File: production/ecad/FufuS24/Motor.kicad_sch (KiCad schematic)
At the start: 8 parts, among them J10 Conn_01x02, J12 Conn_01x02, J13 Conn_01x03_Socket, J5 691137710004, U12 Pololu_DRV8711_Motor_Driver

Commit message: efan 8
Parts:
- J13: footprint (none) -> footprints:HDMI_A
- J5: footprint 691137710004:WURTH_691137710004 -> footprints:PWR_4POS
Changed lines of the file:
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@@
       (effects (font (size 1.27 1.27)))
     )
-    (property "Footprint" "" (at 94.615 49.53 0)
+    (property "Footprint" "footprints:HDMI_A" (at 94.615 49.53 0)
       (effects (font (size 1.27 1.27)) hide)
     )
@@
       (effects (font (size 1.27 1.27)))
     )
-    (property "Footprint" "691137710004:WURTH_691137710004" (at 103.505 92.71 0)
+    (property "Footprint" "footprints:PWR_4POS" (at 103.505 92.71 0)
       (effects (font (size 1.27 1.27)) (justify bottom) hide)
     )

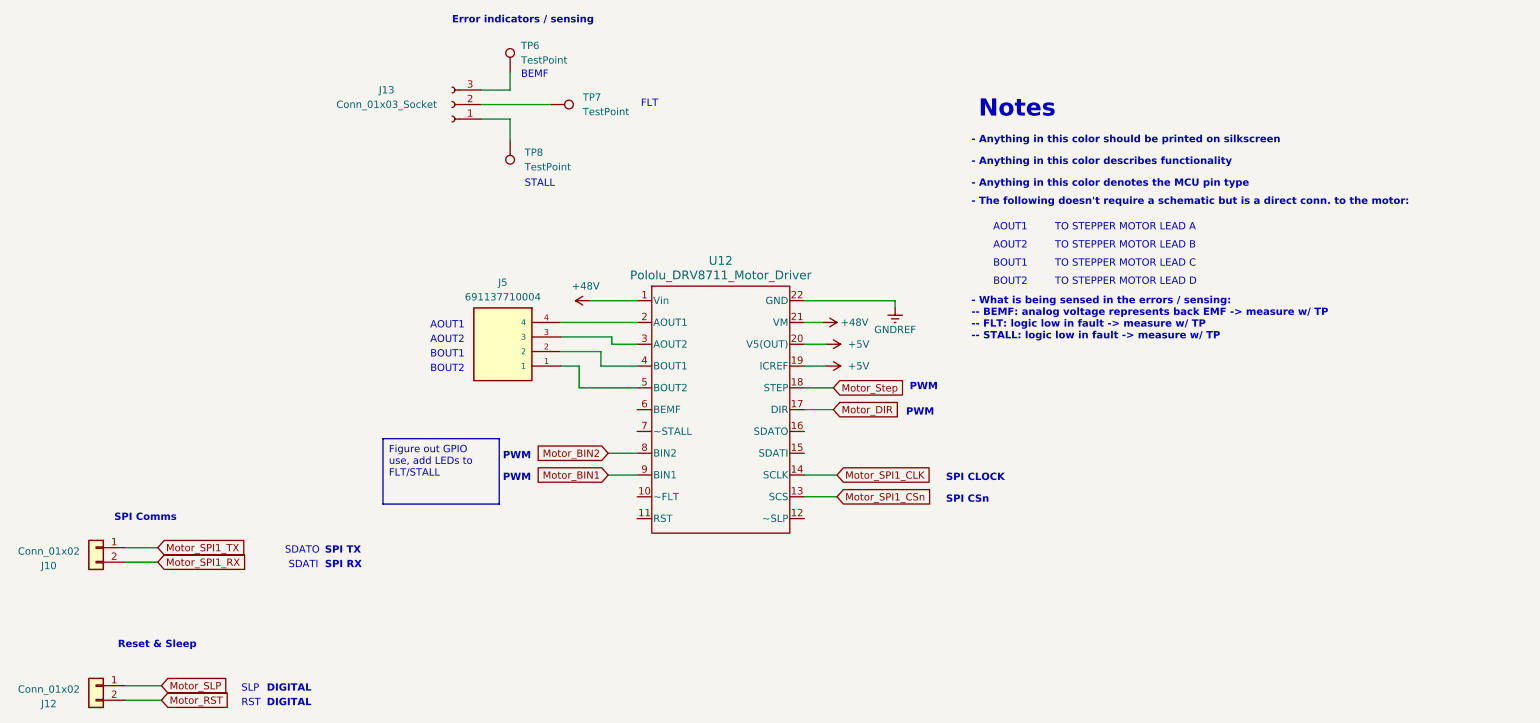
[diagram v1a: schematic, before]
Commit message: Update Motor.kicad_sch
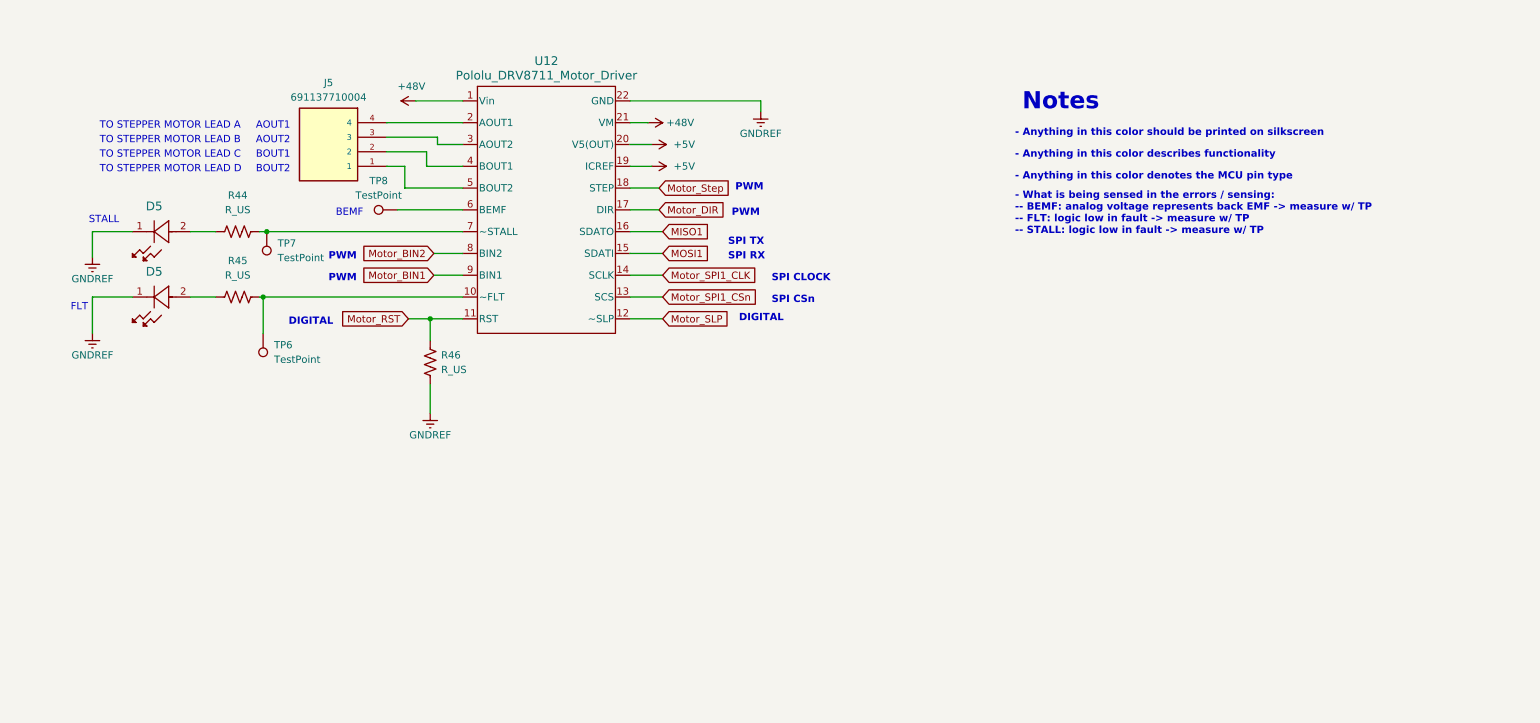
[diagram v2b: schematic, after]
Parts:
- removed J10, J12: Conn_01x02, footprints:CON_5025840270_MOL, symbol Connector_Generic:Conn_01x02
- removed J13: Conn_01x03_Socket, footprints:HDMI_A, symbol Connector:Conn_01x03_Socket
- added D5 (x2): 150080GS75000, LED_GS75000_WRE, symbol 150080GS75000:150080GS75000
- added R44, R45, R46: R_US, symbol Device:R_US
- J5: footprint footprints:PWR_4POS -> 691137710004:WURTH_691137710004
- TP6, TP7, TP8: footprint footprints:TP_5014 -> TestPoint:TestPoint_Pad_2.0x2.0mm
- U12: footprint footprints:POLOLU_36v4 -> (none)
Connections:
- net GNDREF: now also D5.1, D5.1, R46.2
- net Motor_RST: now also U12.11 (RST), R46.1
- net Motor_SLP: now also U12.12 (~SLP)
- net at TP7.1: now also U12.7 (~STALL), R44.1
- net at TP8.1: now also U12.6 (BEMF)
- net at TP6.1: now also U12.10 (~FLT), R45.1
- net MOSI1: now reaches U12.15 (SDATI)
- net MISO1: now reaches U12.16 (SDATO)
- new net: D5.2, R44.2
- new net: D5.2, R45.2
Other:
- note removed: "- The following doesn't require a schematic but is a direct conn. to the motor:"
- note removed: "Error indicators / sensing"
- note removed: "RST"
- note removed: "Reset & Sleep"
- note removed: "SDATI"
- note removed: "SDATO"
- note removed: "SLP"
- note removed: "SPI Comms"

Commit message: efan 9
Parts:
- renumbered D5 to D10, D5 to D11
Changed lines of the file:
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@@
           (reference "#PWR090") (unit 1)
         )
-        (path "/c4c3980b-c8c0-435e-abdc-bbed2349d7ac/4167d6e6-5417-44cf-9a0c-baf8fab8b739"
-          (reference "#PWR086") (unit 1)
-        )
       )
     )
@@
         (path "/c4c3980b-c8c0-435e-abdc-bbed2349d7ac/67add6e2-1584-4801-9b59-67cf5082dcca"
           (reference "R44") (unit 1)
-        )
-        (path "/c4c3980b-c8c0-435e-abdc-bbed2349d7ac/4167d6e6-5417-44cf-9a0c-baf8fab8b739"
-          (reference "R29") (unit 1)
         )
       )
@@
           (reference "#PWR080") (unit 1)
         )
-        (path "/c4c3980b-c8c0-435e-abdc-bbed2349d7ac/4167d6e6-5417-44cf-9a0c-baf8fab8b739"
-          (reference "#PWR082") (unit 1)
-        )
       )
     )
@@
         (path "/c4c3980b-c8c0-435e-abdc-bbed2349d7ac/67add6e2-1584-4801-9b59-67cf5082dcca"
           (reference "TP7") (unit 1)
-        )
-        (path "/c4c3980b-c8c0-435e-abdc-bbed2349d7ac/4167d6e6-5417-44cf-9a0c-baf8fab8b739"
-          (reference "TP14") (unit 1)
         )
       )
@@
           (reference "U12") (unit 1)
         )
-        (path "/c4c3980b-c8c0-435e-abdc-bbed2349d7ac/4167d6e6-5417-44cf-9a0c-baf8fab8b739"
-          (reference "U13") (unit 1)
-        )
       )
     )
@@
         (path "/c4c3980b-c8c0-435e-abdc-bbed2349d7ac/67add6e2-1584-4801-9b59-67cf5082dcca"
           (reference "TP8") (unit 1)
-        )
-        (path "/c4c3980b-c8c0-435e-abdc-bbed2349d7ac/4167d6e6-5417-44cf-9a0c-baf8fab8b739"
-          (reference "TP15") (unit 1)
         )
       )
@@
         (path "/c4c3980b-c8c0-435e-abdc-bbed2349d7ac/67add6e2-1584-4801-9b59-67cf5082dcca"
           (reference "#PWR088") (unit 1)
-        )
-        (path "/c4c3980b-c8c0-435e-abdc-bbed2349d7ac/4167d6e6-5417-44cf-9a0c-baf8fab8b739"
-          (reference "#PWR084") (unit 1)
         )
       )
@@
           (reference "#PWR078") (unit 1)
         )
-        (path "/c4c3980b-c8c0-435e-abdc-bbed2349d7ac/4167d6e6-5417-44cf-9a0c-baf8fab8b739"
-          (reference "#PWR059") (unit 1)
-        )
       )
     )
@@
           (reference "R46") (unit 1)
         )
-        (path "/c4c3980b-c8c0-435e-abdc-bbed2349d7ac/4167d6e6-5417-44cf-9a0c-baf8fab8b739"
-          (reference "R43") (unit 1)
-        )
       )
     )
@@
   (symbol (lib_id "150080GS75000:150080GS75000") (at 48.895 71.755 180) (unit 1)
     (in_bom yes) (on_board yes) (dnp no) (fields_autoplaced)
-    (property "Reference" "D5" (at 42.545 67.31 0)
+    (property "Reference" "D10" (at 42.545 67.31 0)
       (effects (font (size 1.524 1.524)))
     )
@@
     (instances
       (project "FufuS24"
-        (path "/c4c3980b-c8c0-435e-abdc-bbed2349d7ac/1f62379a-1fa8-439b-93cd-7c736b3b1bba"
-          (reference "D5") (unit 1)
-        )
         (path "/c4c3980b-c8c0-435e-abdc-bbed2349d7ac/67add6e2-1584-4801-9b59-67cf5082dcca"
           (reference "D10") (unit 1)
         )
-        (path "/c4c3980b-c8c0-435e-abdc-bbed2349d7ac/4167d6e6-5417-44cf-9a0c-baf8fab8b739"
-          (reference "D8") (unit 1)
-        )
       )
     )
@@
         (path "/c4c3980b-c8c0-435e-abdc-bbed2349d7ac/67add6e2-1584-4801-9b59-67cf5082dcca"
           (reference "R45") (unit 1)
-        )
-        (path "/c4c3980b-c8c0-435e-abdc-bbed2349d7ac/4167d6e6-5417-44cf-9a0c-baf8fab8b739"
-          (reference "R30") (unit 1)
         )
       )
@@
         (path "/c4c3980b-c8c0-435e-abdc-bbed2349d7ac/67add6e2-1584-4801-9b59-67cf5082dcca"
           (reference "#PWR087") (unit 1)
-        )
-        (path "/c4c3980b-c8c0-435e-abdc-bbed2349d7ac/4167d6e6-5417-44cf-9a0c-baf8fab8b739"
-          (reference "#PWR083") (unit 1)
         )
       )
@@
           (reference "J5") (unit 1)
         )
-        (path "/c4c3980b-c8c0-435e-abdc-bbed2349d7ac/4167d6e6-5417-44cf-9a0c-baf8fab8b739"
-          (reference "J6") (unit 1)
-        )
       )
     )
@@
         (path "/c4c3980b-c8c0-435e-abdc-bbed2349d7ac/67add6e2-1584-4801-9b59-67cf5082dcca"
           (reference "TP6") (unit 1)
-        )
-        (path "/c4c3980b-c8c0-435e-abdc-bbed2349d7ac/4167d6e6-5417-44cf-9a0c-baf8fab8b739"
-          (reference "TP13") (unit 1)
         )
       )
@@
           (reference "#PWR077") (unit 1)
         )
-        (path "/c4c3980b-c8c0-435e-abdc-bbed2349d7ac/4167d6e6-5417-44cf-9a0c-baf8fab8b739"
-          (reference "#PWR058") (unit 1)
-        )
       )
     )
@@
   (symbol (lib_id "150080GS75000:150080GS75000") (at 48.895 83.185 180) (unit 1)
     (in_bom yes) (on_board yes) (dnp no) (fields_autoplaced)
-    (property "Reference" "D5" (at 42.545 78.74 0)
+    (property "Reference" "D11" (at 42.545 78.74 0)
       (effects (font (size 1.524 1.524)))
     )
@@
     (instances
       (project "FufuS24"
-        (path "/c4c3980b-c8c0-435e-abdc-bbed2349d7ac/1f62379a-1fa8-439b-93cd-7c736b3b1bba"
-          (reference "D5") (unit 1)
-        )
         (path "/c4c3980b-c8c0-435e-abdc-bbed2349d7ac/67add6e2-1584-4801-9b59-67cf5082dcca"
           (reference "D11") (unit 1)
-        )
-        (path "/c4c3980b-c8c0-435e-abdc-bbed2349d7ac/4167d6e6-5417-44cf-9a0c-baf8fab8b739"
-          (reference "D9") (unit 1)
         )
       )
@@
           (reference "#PWR079") (unit 1)
         )
-        (path "/c4c3980b-c8c0-435e-abdc-bbed2349d7ac/4167d6e6-5417-44cf-9a0c-baf8fab8b739"
-          (reference "#PWR081") (unit 1)
-        )
       )
     )
@@
           (reference "#PWR089") (unit 1)
         )
-        (path "/c4c3980b-c8c0-435e-abdc-bbed2349d7ac/4167d6e6-5417-44cf-9a0c-baf8fab8b739"
-          (reference "#PWR085") (unit 1)
-        )
-      )
+      )

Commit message: Footprints
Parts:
- D10, D11: footprint LED_GS75000_WRE -> footprints:LED_GS75000_WRE
- J5: footprint 691137710004:WURTH_691137710004 -> footprints:PWR_4POS
- R44, R45, R46: footprint (none) -> footprints:RESC2012X60N
- TP6, TP7, TP8: footprint TestPoint:TestPoint_Pad_2.0x2.0mm -> footprints:TP_5014
- U12: footprint (none) -> footprints:POLOLU_36v4
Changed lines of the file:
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@@
       (effects (font (size 1.27 1.27)))
     )
-    (property "Footprint" "" (at 56.896 72.771 90)
+    (property "Footprint" "footprints:RESC2012X60N" (at 56.896 72.771 90)
       (effects (font (size 1.27 1.27)) hide)
     )
@@
       (effects (font (size 1.27 1.27)) (justify right))
     )
-    (property "Footprint" "TestPoint:TestPoint_Pad_2.0x2.0mm" (at 57.15 71.755 0)
+    (property "Footprint" "footprints:TP_5014" (at 57.15 71.755 0)
       (effects (font (size 1.27 1.27)) hide)
     )
@@
       (effects (font (size 1.524 1.524)))
     )
-    (property "Footprint" "" (at 88.9 43.815 0)
+    (property "Footprint" "footprints:POLOLU_36v4" (at 88.9 43.815 0)
       (effects (font (size 1.27 1.27) italic) hide)
     )
@@
       (effects (font (size 1.27 1.27)))
     )
-    (property "Footprint" "TestPoint:TestPoint_Pad_2.0x2.0mm" (at 85.09 62.865 0)
+    (property "Footprint" "footprints:TP_5014" (at 85.09 62.865 0)
       (effects (font (size 1.27 1.27)) hide)
     )
@@
       (effects (font (size 1.27 1.27)) (justify left))
     )
-    (property "Footprint" "" (at 91.821 94.869 90)
+    (property "Footprint" "footprints:RESC2012X60N" (at 91.821 94.869 90)
       (effects (font (size 1.27 1.27)) hide)
     )
@@
       (effects (font (size 1.524 1.524)) (justify left) hide)
     )
-    (property "Footprint" "LED_GS75000_WRE" (at 50.165 76.835 0)
+    (property "Footprint" "footprints:LED_GS75000_WRE" (at 50.165 76.835 0)
       (effects (font (size 1.27 1.27) italic) hide)
     )
@@
       (effects (font (size 1.27 1.27)))
     )
-    (property "Footprint" "" (at 56.896 84.201 90)
+    (property "Footprint" "footprints:RESC2012X60N" (at 56.896 84.201 90)
       (effects (font (size 1.27 1.27)) hide)
     )
@@
       (effects (font (size 1.27 1.27)))
     )
-    (property "Footprint" "691137710004:WURTH_691137710004" (at 73.025 57.785 0)
+    (property "Footprint" "footprints:PWR_4POS" (at 73.025 57.785 0)
       (effects (font (size 1.27 1.27)) (justify bottom) hide)
     )
@@
       (effects (font (size 1.27 1.27)) (justify right))
     )
-    (property "Footprint" "TestPoint:TestPoint_Pad_2.0x2.0mm" (at 56.515 89.535 0)
+    (property "Footprint" "footprints:TP_5014" (at 56.515 89.535 0)
       (effects (font (size 1.27 1.27)) hide)
     )
@@
       (effects (font (size 1.524 1.524)) (justify left) hide)
     )
-    (property "Footprint" "LED_GS75000_WRE" (at 50.165 88.265 0)
-      (effects (font (size 1.27 1.27) italic) hide)
-    )
+    (property "Footprint" "footprints:LED_GS75000_WRE" (at 50.165 88.265 0)
+      (effects (font (size 1.27 1.27) italic) hide)
+    )

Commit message: efan finals before laying out
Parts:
- removed TP6, TP7, TP8: TestPoint, footprints:TP_5014, symbol Connector:TestPoint
- added TP6, TP7, TP8: 5014, footprints:TP_5014, symbol 5014:5014
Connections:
- net at R44.1, U12.7 (~STALL): now also TP7.TP
- net at R45.1, U12.10 (~FLT): now also TP6.TP
- net at U12.6 (BEMF): now also TP8.TP

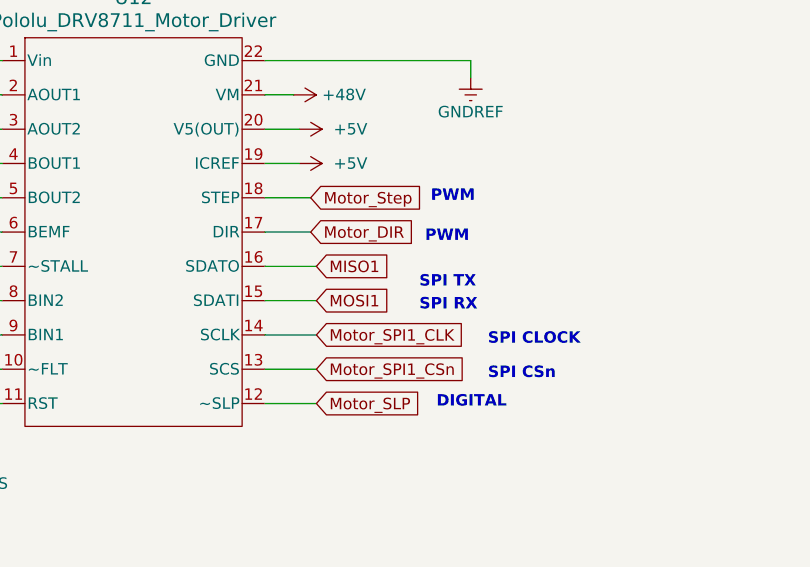
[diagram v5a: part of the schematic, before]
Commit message: major layout changes
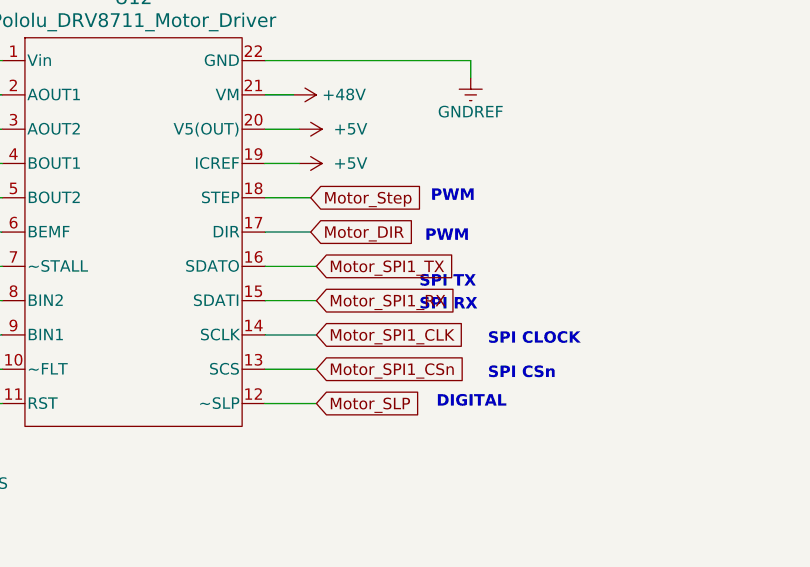
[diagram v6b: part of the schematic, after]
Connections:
- net MISO1 renamed Motor_SPI1_TX
- net MOSI1 renamed Motor_SPI1_RX
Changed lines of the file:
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@@
     )
   )
-  (global_label "MISO1" (shape input) (at 131.445 71.755 0) (fields_autoplaced)
+  (global_label "Motor_SPI1_TX" (shape input) (at 131.445 71.755 0) (fields_autoplaced)
     (effects (font (size 1.27 1.27)) (justify left))
-    (property "Intersheetrefs" "${INTERSHEET_REFS}" (at 140.2359 71.755 0)
+    (property "Intersheetrefs" "${INTERSHEET_REFS}" (at 148.0976 71.755 0)
       (effects (font (size 1.27 1.27)) (justify left) hide)
     )
   )
-  (global_label "MOSI1" (shape input) (at 131.445 75.565 0) (fields_autoplaced)
+  (global_label "Motor_SPI1_RX" (shape input) (at 131.445 75.565 0) (fields_autoplaced)
     (effects (font (size 1.27 1.27)) (justify left))
-    (property "Intersheetrefs" "${INTERSHEET_REFS}" (at 140.2359 75.565 0)
+    (property "Intersheetrefs" "${INTERSHEET_REFS}" (at 148.4 75.565 0)
       (effects (font (size 1.27 1.27)) (justify left) hide)
     )

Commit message: i am pulling my hair out
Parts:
- removed D10, D11: 150080GS75000, footprints:LED_GS75000_WRE, symbol 150080GS75000:150080GS75000
- removed R44, R45, R46: R_US, footprints:RESC2012X60N, symbol Device:R_US
- removed TP6, TP7, TP8: 5014, footprints:TP_5014, symbol 5014:5014
- removed U12: Pololu_DRV8711_Motor_Driver, footprints:POLOLU_36v4, symbol POLOLU_35v4:Pololu_DRV8711_Motor_Driver
- added R26: TBD, footprints:RESC2012X60N, symbol Device:R_US
- added U3: TXS0101DBVR, TXS0101DBVR:SOT95P280X145-6N, symbol LevelShifter_Motor:TXS0101DBVR
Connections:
- net +48V: now also J5.1
- net +5V: now also U3.6 (VCCB)
- net GNDREF: now also R26.2, U3.2 (GND)
- net at J5.4: now also U3.4 (B)
- net GPIO_3: now reaches J5.3
- net GPIO_4: now reaches J5.2
- new net +3.3V: R26.1, U3.1 (VCCA), U3.5 (OE)
- new net Motor_PWM: U3.3 (A)
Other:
- note removed: "- Anything in this color denotes the MCU pin type"
- note removed: "- Anything in this color describes functionality"
- note removed: "- Anything in this color should be printed on silkscreen"
- note removed: "- What is being sensed in the errors / sensing: -- BEMF: analog voltage represents back EMF -> measure w/ TP -- FLT: logic low in fault -> measure w/ TP -- STALL: logic low in fault -> measure w/ TP"
- note removed: "AOUT1"
- note removed: "AOUT2"
- note removed: "BEMF"
- note removed: "BOUT1"
- note removed: "BOUT2"
- note removed: "DIGITAL"
- note removed: "FLT"
- note removed: "Notes"
- note removed: "PWM"
- note removed: "SPI CLOCK"
- note removed: "SPI CSn"
- note removed: "SPI RX"
- note removed: "SPI TX"
- note removed: "STALL"
- note removed: "TO STEPPER MOTOR LEAD A"
- note removed: "TO STEPPER MOTOR LEAD B"
- note removed: "TO STEPPER MOTOR LEAD C"
- note removed: "TO STEPPER MOTOR LEAD D"
- moved on the sheet: J5

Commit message: changes
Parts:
- added C40, C41: 100n, footprints:WCAP-CSGP_885012206026, symbol Device:C
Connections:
- net +3.3V: now also C40.1
- net +5V: now also C41.1
- net GNDREF: now also C40.2, C41.2
